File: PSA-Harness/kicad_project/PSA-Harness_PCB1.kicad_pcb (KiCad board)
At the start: 4 copper layers, 22.4 x 43.8 mm, 5 parts, among them J10 B2B_1, J11 B2B_2, J4 to_car_1, J5 to_car_2, J6 to_car_3

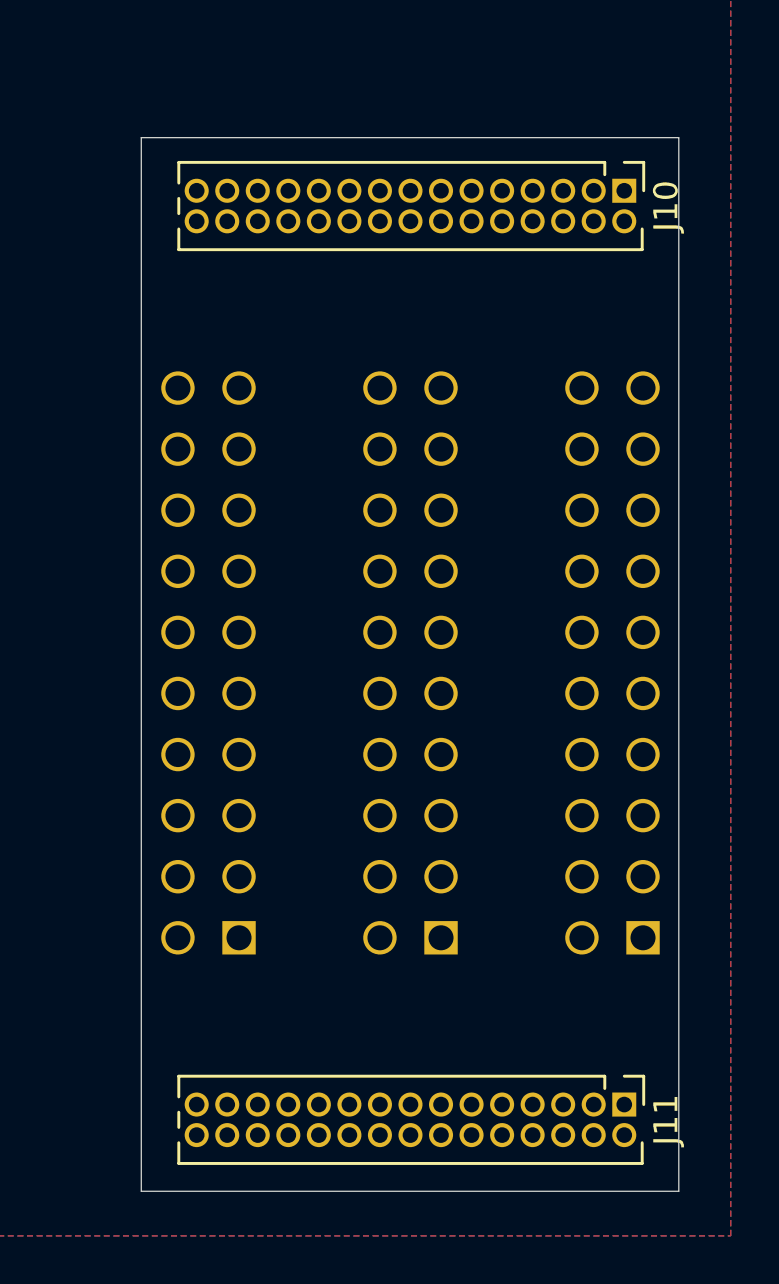
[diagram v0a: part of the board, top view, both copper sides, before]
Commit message: PCB1 routed, PCB2 partly routed
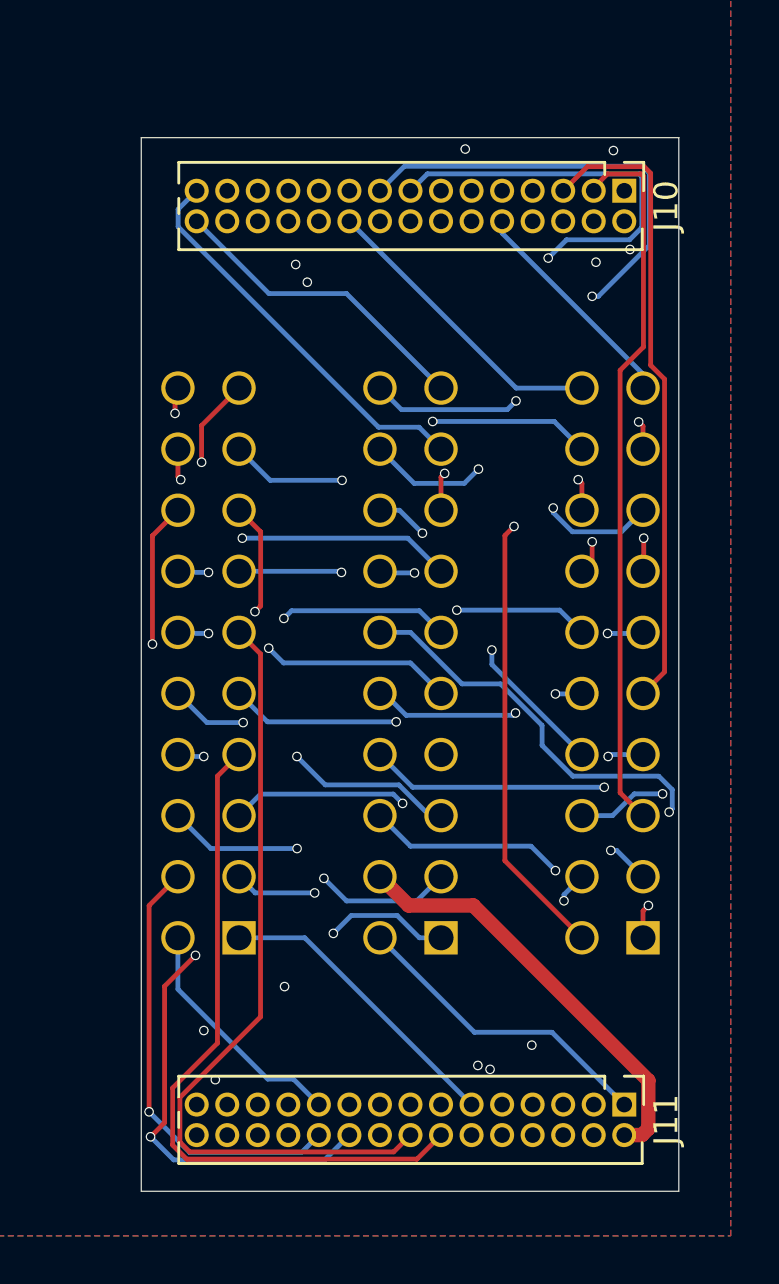
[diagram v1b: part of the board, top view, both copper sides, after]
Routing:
- net 11: track 0.00 -> 56.3 mm, vias 0 -> 2
- net 40: track 0.00 -> 48.5 mm, vias 0 -> 2
- net 21: track 0.00 -> 48.3 mm, vias 0 -> 2
- net 50: track 0.00 -> 41.8 mm, vias 0 -> 3
- net 48: track 0.00 -> 40.8 mm, vias 0 -> 2
- net 38: track 0.00 -> 40.2 mm, vias 0 -> 2
- net 23: track 0.00 -> 39.8 mm, vias 0 -> 2
- net 13: track 0.00 -> 39.3 mm, vias 0 -> 2
- net 15: track 0.00 -> 36.0 mm, vias 0 -> 2
- net 36: track 0.00 -> 35.0 mm, vias 0 -> 1
- net 25: track 0.00 -> 33.3 mm, vias 0 -> 1
- net 22: track 0.00 -> 33.1 mm, vias 0 -> 1
- net CAN1_H: track 0.00 -> 33.0 mm
- net 42: track 0.00 -> 32.6 mm, vias 0 -> 1
- net 19: track 0.00 -> 32.1 mm, vias 0 -> 1
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
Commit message: chg: rearrange pcb interconnect pins
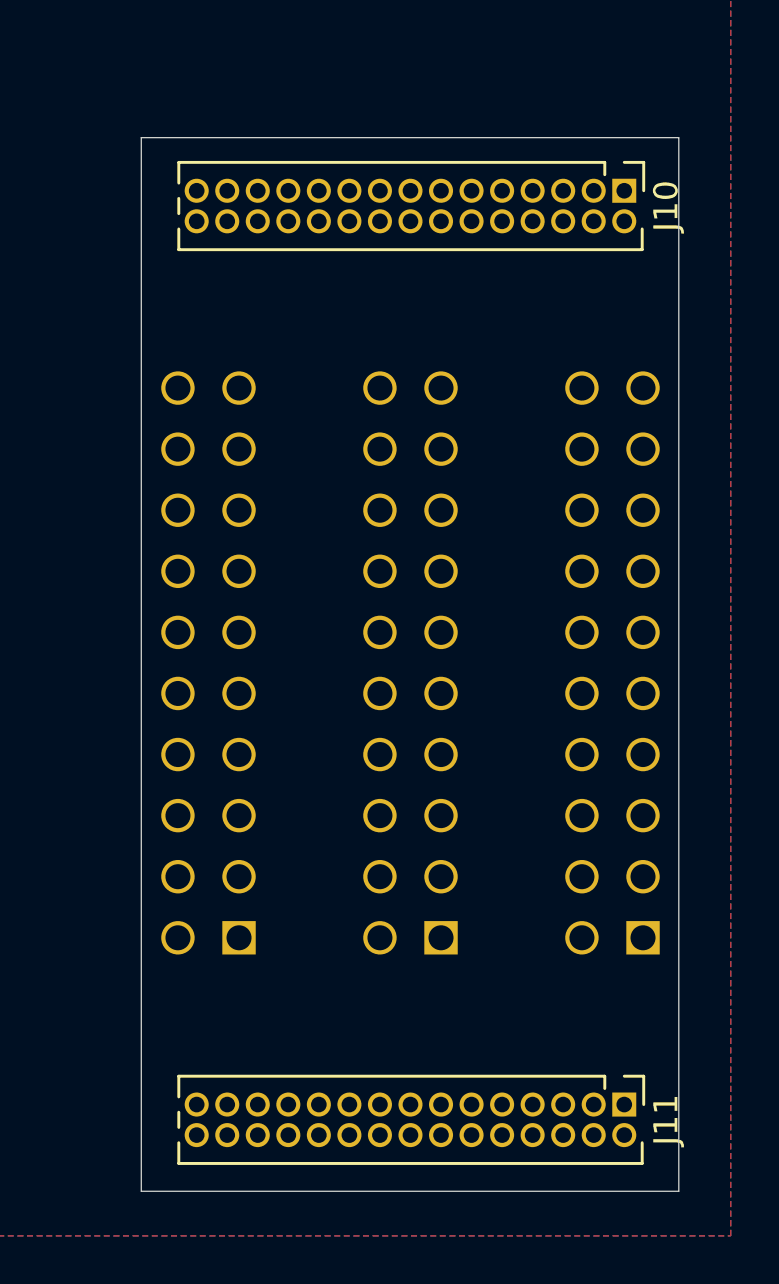
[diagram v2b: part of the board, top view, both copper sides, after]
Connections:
- J10 pad 1: 1 -> 11
- J10 pad 10: 10 -> 16
- J10 pad 11: 11 -> 6
- J10 pad 12: 12 -> 17
- J10 pad 13: 13 -> 4
- J10 pad 14: 14 -> 18
- J10 pad 15: 15 -> 2
- J10 pad 16: 16 -> 19
- J10 pad 17: 17 -> 1
- J10 pad 18: 18 -> 20
- J10 pad 19: 19 -> CAN2_H
- J10 pad 2: 2 -> 12
- J10 pad 20: 20 -> 21
- J10 pad 21: 21 -> CAN2_L
- J10 pad 23: 23 -> CAN1_H
- J10 pad 24: GND -> 23
- J10 pad 25: 25 -> CAN1_L
- J10 pad 26: 26 -> 25
- J10 pad 27: 27 -> GND
- J10 pad 28: 28 -> 26
- J10 pad 29: 29 -> +12V
- J10 pad 3: CAN2_L -> 10
- J10 pad 30: 30 -> 27
- J10 pad 4: 4 -> 13
- J10 pad 5: CAN2_H -> 9
- J10 pad 6: 6 -> 14
- J10 pad 7: 7 -> 8
- J10 pad 8: 8 -> 15
- J10 pad 9: 9 -> 7
- J11 pad 1: 31 -> 43
- J11 pad 10: 40 -> 50
- J11 pad 11: 41 -> 38
- J11 pad 12: 42 -> 51
- J11 pad 13: 43 -> 37
- J11 pad 14: CAN1_L -> 52
- J11 pad 15: 45 -> 36
- J11 pad 16: CAN1_H -> 53
- J11 pad 17: 47 -> 35
- J11 pad 18: 48 -> 54
- J11 pad 19: 49 -> 34
- J11 pad 2: +12V -> 45
- J11 pad 20: 50 -> 55
- J11 pad 21: 51 -> 33
- J11 pad 22: 52 -> 56
- J11 pad 23: 53 -> 31
- J11 pad 24: 54 -> 57
- J11 pad 25: 55 -> 30
- J11 pad 26: 56 -> 58
- J11 pad 27: 57 -> 29
- J11 pad 28: 58 -> 59
- J11 pad 29: 59 -> 28
- J11 pad 3: 33 -> 42
- J11 pad 4: 34 -> 47
- J11 pad 5: 35 -> 41
- J11 pad 6: 36 -> 48
- J11 pad 7: 37 -> 40
- J11 pad 8: 38 -> 49
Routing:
- net 11: track 56.3 -> 0.00 mm, vias 2 -> 0
- net 40: track 48.5 -> 0.00 mm, vias 2 -> 0
- net 21: track 48.3 -> 0.00 mm, vias 2 -> 0
- net 50: track 41.8 -> 0.00 mm, vias 3 -> 0
- net 48: track 40.8 -> 0.00 mm, vias 2 -> 0
- net 38: track 40.2 -> 0.00 mm, vias 2 -> 0
- net 23: track 39.8 -> 0.00 mm, vias 2 -> 0
- net 13: track 39.3 -> 0.00 mm, vias 2 -> 0
- net 15: track 36.0 -> 0.00 mm, vias 2 -> 0
- net 36: track 35.0 -> 0.00 mm, vias 1 -> 0
- net 25: track 33.3 -> 0.00 mm, vias 1 -> 0
- net 22: track 33.1 -> 0.00 mm, vias 1 -> 0
- net CAN1_H: track 33.0 -> 0.00 mm
- net 42: track 32.6 -> 0.00 mm, vias 1 -> 0
- net 19: track 32.1 -> 0.00 mm, vias 1 -> 0
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
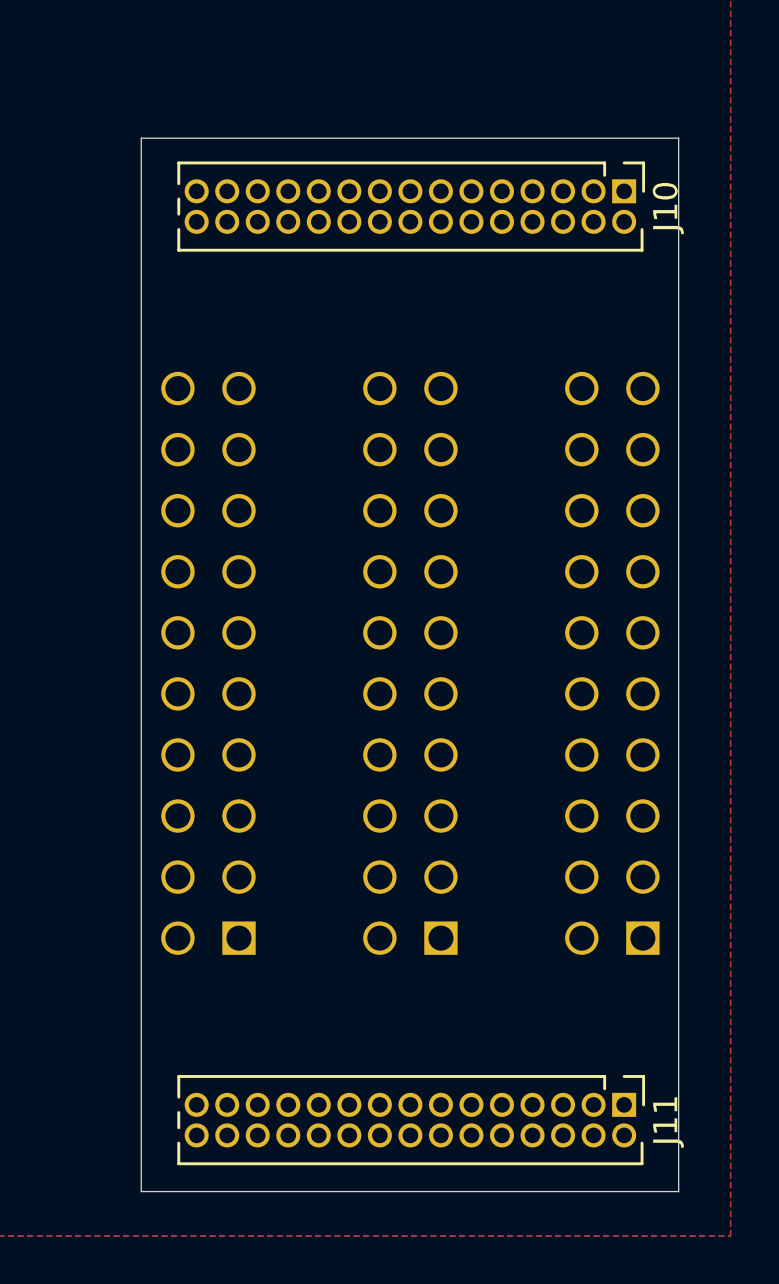
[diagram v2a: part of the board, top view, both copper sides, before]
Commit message: PCB1 routed, PCB2 partly
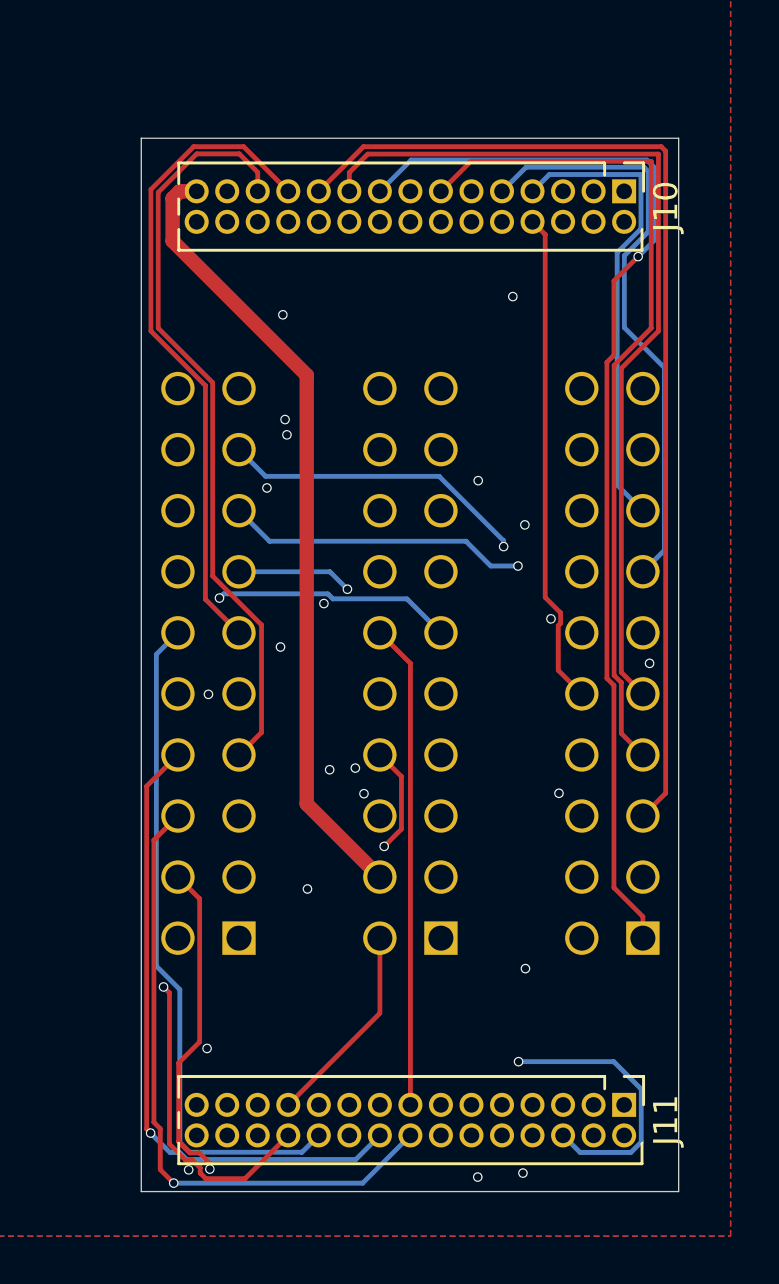
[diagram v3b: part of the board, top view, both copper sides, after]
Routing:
- net 50: track 0.00 -> 51.3 mm, vias 0 -> 2
- net 2: track 0.00 -> 49.6 mm, vias 0 -> 2
- net 49: track 0.00 -> 47.5 mm, vias 0 -> 3
- net 1: track 0.00 -> 45.6 mm, vias 0 -> 1
- net 48: track 0.00 -> 44.8 mm, vias 0 -> 2
- net CAN2_L: track 0.00 -> 43.3 mm
- net 47: track 0.00 -> 41.7 mm, vias 0 -> 2
- net CAN2_H: track 0.00 -> 37.4 mm
- net 11: track 0.00 -> 36.4 mm, vias 0 -> 1
- net 30: track 0.00 -> 35.7 mm, vias 0 -> 1
- net 4: track 0.00 -> 35.1 mm
- net 21: track 0.00 -> 34.8 mm, vias 0 -> 1
- net 29: track 0.00 -> 34.2 mm, vias 0 -> 1
- net 60: track 0.00 -> 33.0 mm
- net 40: track 0.00 -> 33.0 mm
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
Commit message: PCB1+2 routed
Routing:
- net 52: track 23.9 -> 37.3 mm
- net 4: track 35.1 -> 45.2 mm, vias 0 -> 3
- net 51: track 24.1 -> 33.5 mm, vias 1 -> 0
- net 2: track 49.6 -> 41.0 mm
- net 1: track 45.6 -> 53.2 mm, vias 1 -> 2
- net 23: track 29.1 -> 33.9 mm
- net 42: track 18.7 -> 22.7 mm, vias 0 -> 1
- net 11: track 36.4 -> 32.4 mm
- net 22: track 29.9 -> 33.5 mm
- net 27: track 22.2 -> 18.8 mm, vias 0 -> 1
- net 43: track 21.5 -> 24.7 mm, vias 0 -> 1
- net 28: track 30.5 -> 33.5 mm
- net 40: track 33.0 -> 35.9 mm, vias 0 -> 1
- net 21: track 34.8 -> 32.4 mm
- net 55: track 27.2 -> 29.5 mm
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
